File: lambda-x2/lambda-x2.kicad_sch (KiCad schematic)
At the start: 126 parts, among them J1 FTSH-107-01-F-DV-K, J3 Conn_02x02_Odd_Even, J4 Conn_01x10, P1 33311-24AW-2, Q1 BTS3028, Q2 BTS3028, Q3 BTS3028, Q4 BTS3028, U17 MCP6002T-I/SN, U18 JDY-33, U4 LM78M05_TO252, U5 XC6206P332MR, U6 REF3033, U7 MCP6002T-I/SN, U8 TJA1051T-3

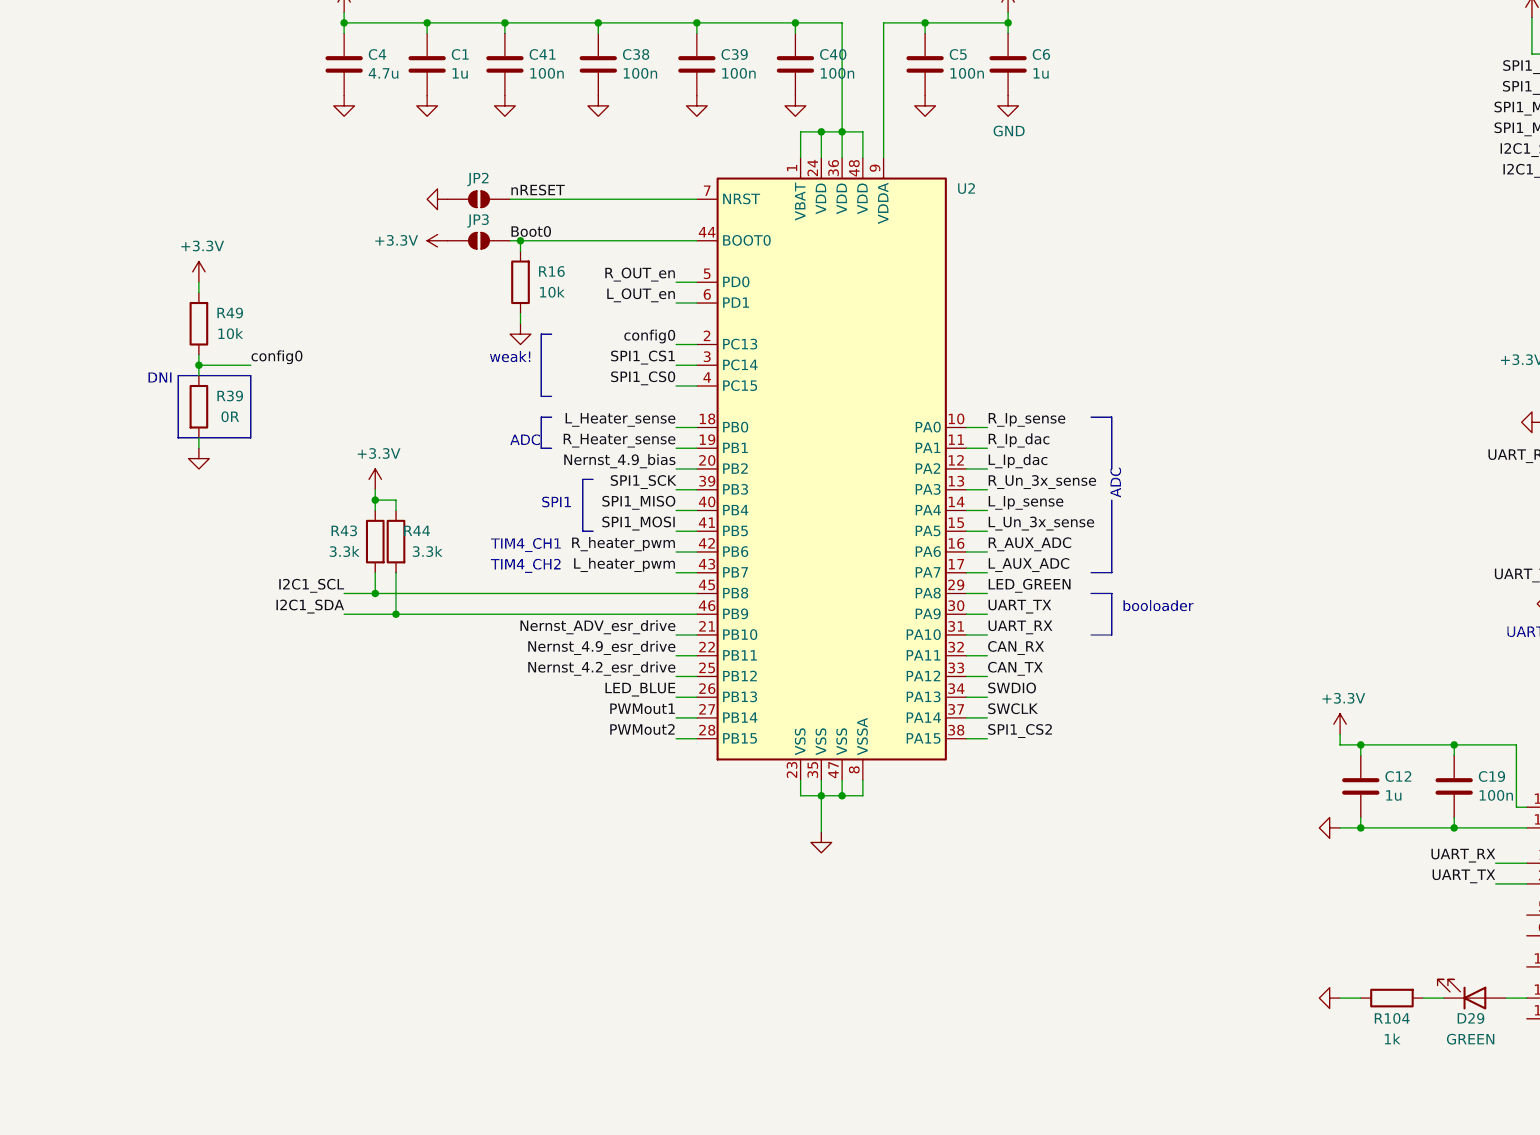
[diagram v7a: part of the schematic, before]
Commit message: lambda-x2: switch to 64-pin MCU
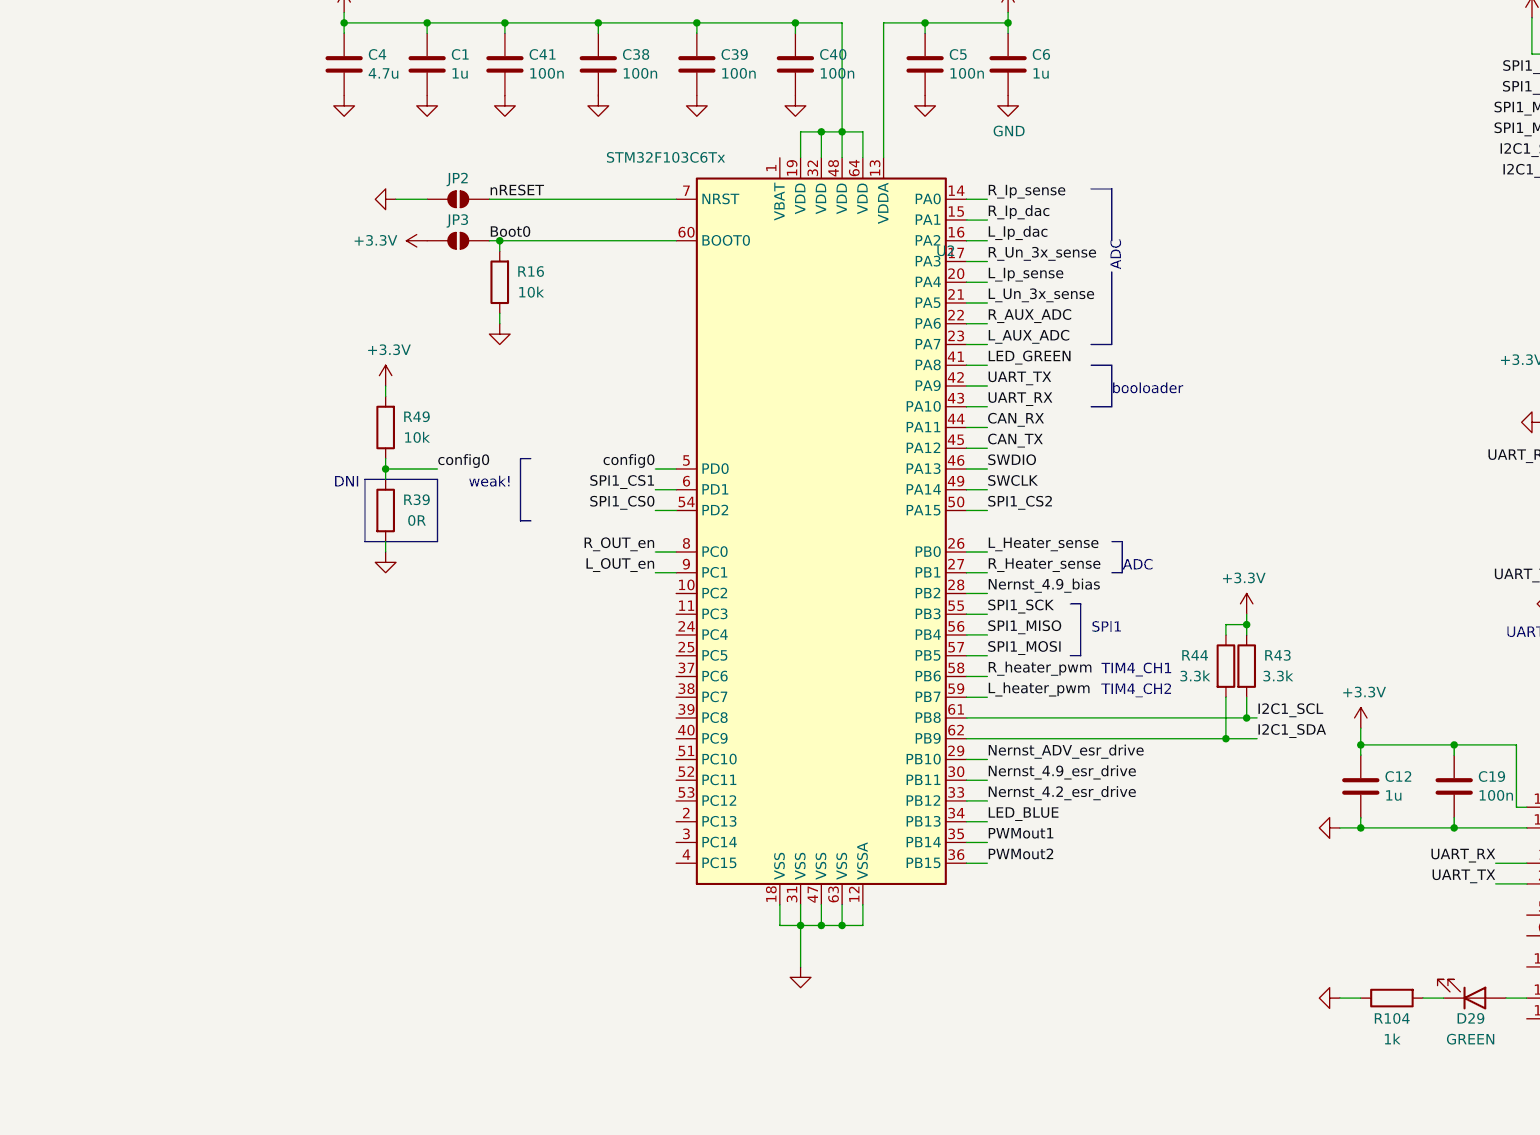
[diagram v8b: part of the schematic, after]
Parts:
- removed U2: (no value), symbol MCU_ST_STM32F1:STM32F103C6Tx
- added U2: STM32F103C6Tx, Package_QFP:LQFP-64_10x10mm_P0.5mm, symbol MCU_ST_STM32F1:STM32F103RCTx
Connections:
- net +3V3: now also U2.19 (VDD), U2.32 (VDD), U2.48 (VDD), U2.64 (VDD)
- net Boot0: now also U2.60 (BOOT0)
- net CAN_RX: now also U2.44 (PA11)
- net CAN_TX: now also U2.45 (PA12)
- net GND: now also U2.12 (VSSA), U2.18 (VSS), U2.31 (VSS), U2.47 (VSS), U2.63 (VSS)
- net I2C1_SCL: now also U2.61 (PB8)
- net I2C1_SDA: now also U2.62 (PB9)
- net LED_BLUE: now also U2.34 (PB13)
- net LED_GREEN: now also U2.41 (PA8)
- net L_AUX_ADC: now also U2.23 (PA7)
- net L_Heater_sense: now also U2.26 (PB0)
- net L_Ip_dac: now also U2.16 (PA2)
- net L_Ip_sense: now also U2.20 (PA4)
- net L_OUT_en: now also U2.9 (PC1)
- net L_Un_3x_sense: now also U2.21 (PA5)
- net L_heater_pwm: now also U2.59 (PB7)
- net Nernst_4.2_esr_drive: now also U2.33 (PB12)
- net Nernst_4.9_bias: now also U2.28 (PB2)
- net Nernst_4.9_esr_drive: now also U2.30 (PB11)
- net Nernst_ADV_esr_drive: now also U2.29 (PB10)
- net PWMout1: now also U2.35 (PB14)
- net PWMout2: now also U2.36 (PB15)
- net R_AUX_ADC: now also U2.22 (PA6)
- net R_Heater_sense: now also U2.27 (PB1)
- net R_Ip_dac: now also U2.15 (PA1)
- net R_Ip_sense: now also U2.14 (PA0)
- net R_OUT_en: now also U2.8 (PC0)
- net R_Un_3x_sense: now also U2.17 (PA3)
- net R_heater_pwm: now also U2.58 (PB6)
- net SPI1_CS0: now also U2.54 (PD2)
- net SPI1_CS1: now also U2.6 (PD1)
- net SPI1_CS2: now also U2.50 (PA15)
- net SPI1_MISO: now also U2.56 (PB4)
- net SPI1_MOSI: now also U2.57 (PB5)
- net SPI1_SCK: now also U2.55 (PB3)
- net SWCLK: now also U2.49 (PA14)
- net SWDIO: now also U2.46 (PA13)
- net UART_RX: now also U2.43 (PA10)
- net UART_TX: now also U2.42 (PA9)
- net VDDA: now also U2.13 (VDDA)
- net config0: now also U2.5 (PD0)
- net nRESET: now also U2.7 (NRST)
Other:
- moved on the sheet: JP2, JP3, R16, R39, R43, R44, R49
